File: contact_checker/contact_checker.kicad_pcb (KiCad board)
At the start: 4 copper layers, 160 x 100 mm, 48 parts, among them J1 DB9_Male_Female_Stack_Mountin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, J10 Conn_01x01_Female, J11 Conn_01x01_Female, J12 Conn_01x01_Female, J13 Conn_Triaxial, J14 Conn_Triaxial, J15 Conn_Triaxial, J16 Conn_Triaxial, J17 Conn_01x01_Female, J18 Conn_01x01_Female, J19 Conn_Triaxial, J2 Conn_02x06_Odd_Even, J20 Conn_01x01_Female, J21 Conn_01x01_Female, J22 Conn_01x01_Female, J23 Conn_01x01_Female, J24 Conn_01x01_Female, J25 Conn_Triaxial, J26 RJ45_Shielded, J27 RJ45_Shielded, J28 Conn_01x08, J29 Conn_02x04_Odd_Even, J3 Conn_Coaxial, J30 Conn_01x03, J31 Conn_02x03_Odd_Even, J32 Conn_02x03_Odd_Even, J33 Conn_Coaxial, J34 Conn_Coaxial, J35 Conn_Coaxial, J36 Conn_01x03, J4 Conn_Triaxial, J5 Conn_01x01_Female, J6 Conn_01x01_Female, J7 Conn_Triaxial, J8 Conn_01x01_Female, J9 Conn_01x01_Female, K1 EC2-5NU, K2 EC2-5NU

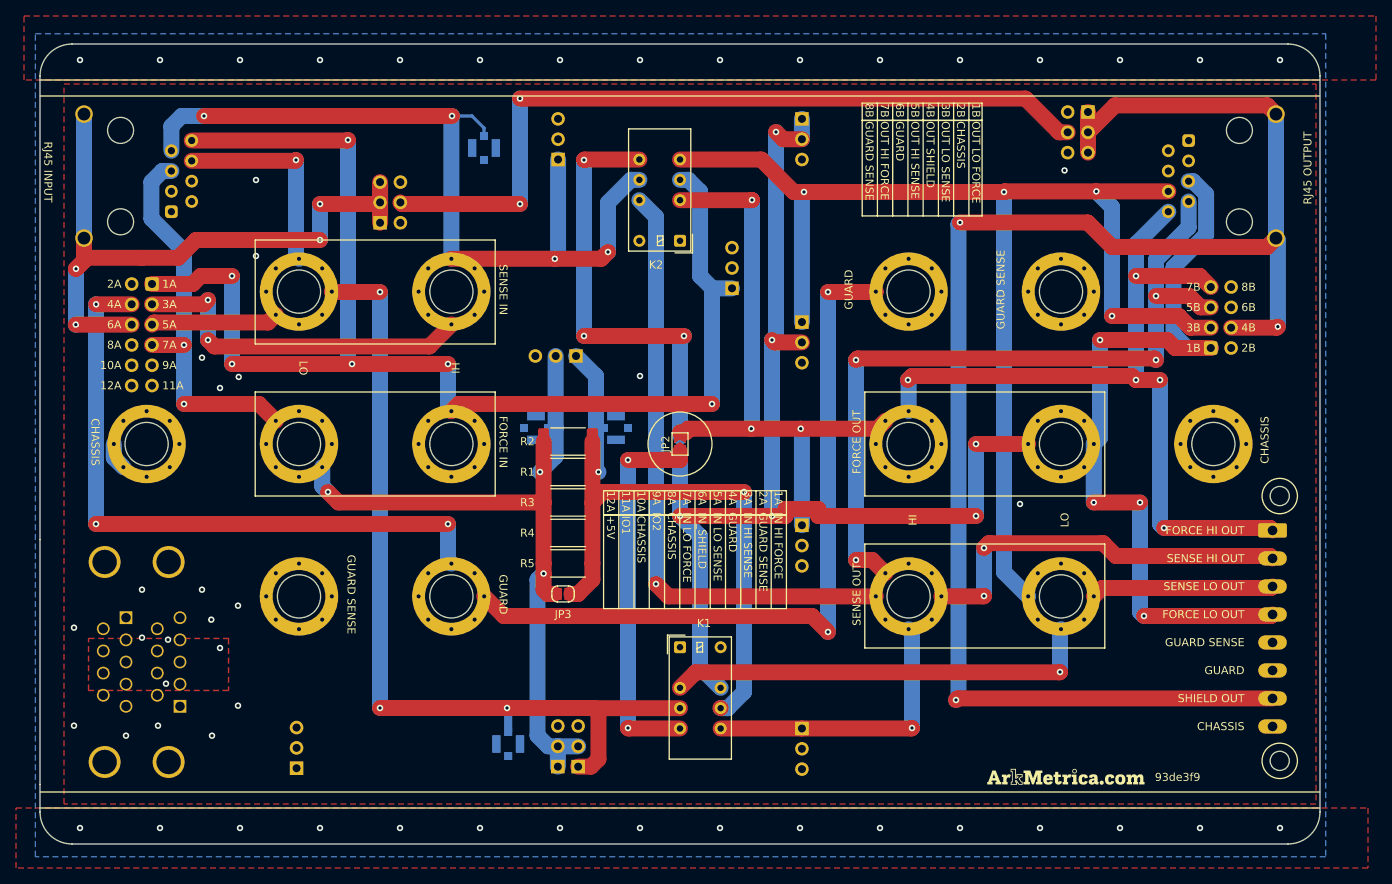
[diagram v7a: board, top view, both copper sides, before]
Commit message: remove banana cons from contact checker
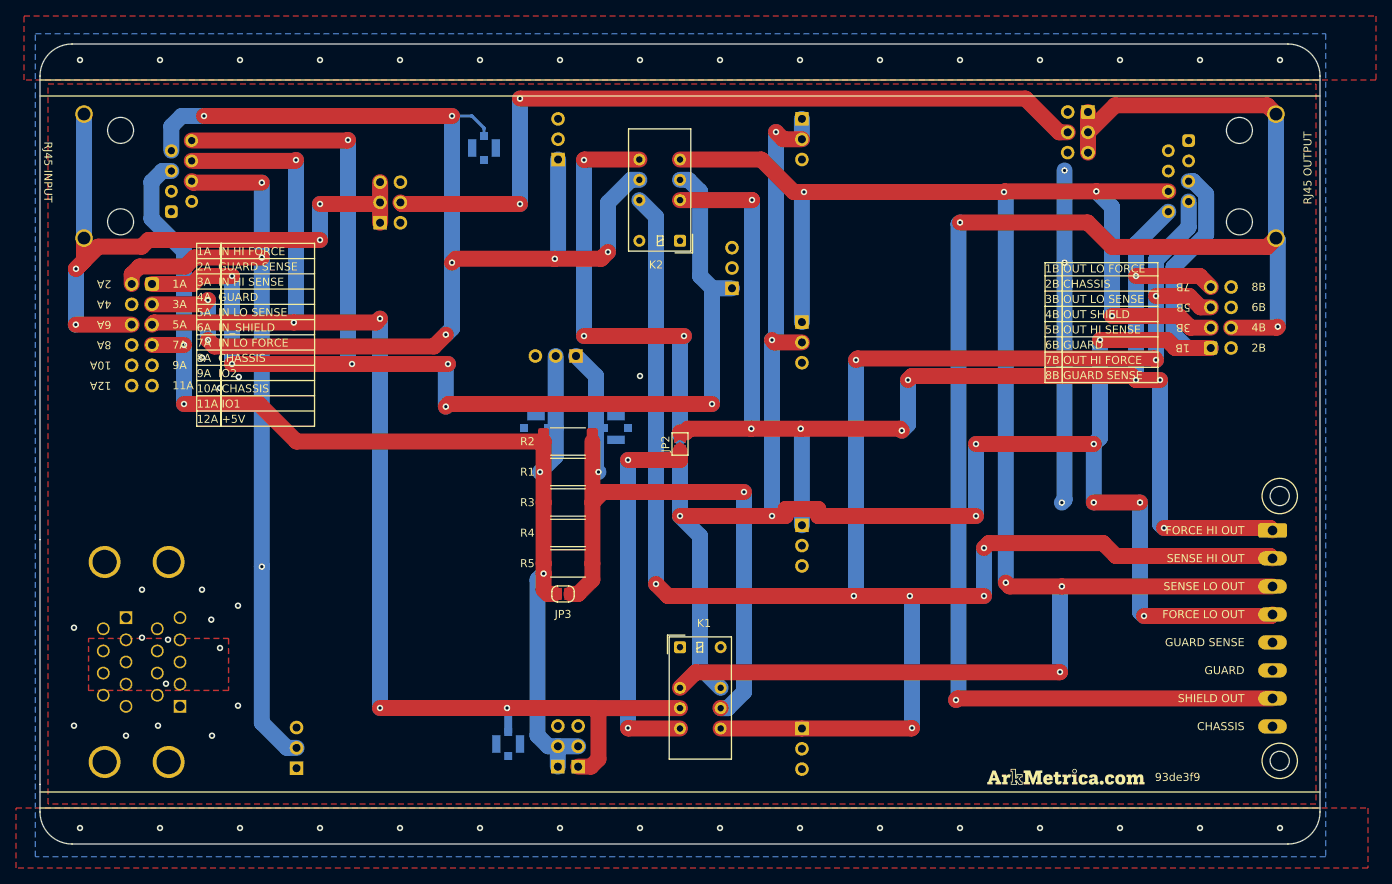
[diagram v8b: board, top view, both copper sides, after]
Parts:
- removed J10, J11, J12, J17, J18, J20, J21, J22, J23, J24, J5, J6, J8, J9: Conn_01x01_Female, custom_footprints:Mounting_Wuerth_WA-SMSI-4.5mm_H3mm_9774030482_pad_mod
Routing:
- net /GUARD: track 174.4 -> 0.00 mm, vias 5 -> 0
- net /GUARD_SENSE: track 316.7 -> 334.4 mm, vias 4 -> 6
- net /OUT_LO_SENSE: track 236.8 -> 250.0 mm, vias 5 -> 7
- net /OUT_HI_SENSE: track 257.8 -> 270.3 mm, vias 8 -> 9
- net /IN_LO_SENSE: track 149.8 -> 161.1 mm, vias 4 -> 5
- net /IN_HI_SENSE: track 150.1 -> 158.7 mm, vias 6 -> 8
- net /OUT_LO_FORCE: track 242.5 -> 250.7 mm, vias 10 -> 11
- net /OUT_HI_FORCE: track 177.0 -> 181.5 mm, vias 8 -> 9
- net /IN_LO_FORCE: track 143.9 -> 147.5 mm, vias 5 -> 4
- net GNDPWR: track 3.40 -> 0.00 mm
- net /IN_HI_FORCE: track 168.0 -> 167.9 mm, vias 6 -> 7
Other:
- board text removed: "FORCE IN"
- board text removed: "FORCE OUT"
- board text removed: "HI"
- board text removed: "LO"
- board text removed: "SENSE IN"
- board text removed: "SENSE OUT"
